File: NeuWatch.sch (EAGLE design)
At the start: 70 parts, among them IC1 SAMD21G18A-AUT, IC3 TPS2115, IC4 SIP32401A, IC5 MC74VHC1G14DFT, T2 2N7002_ALT, Y1 32,768Khz

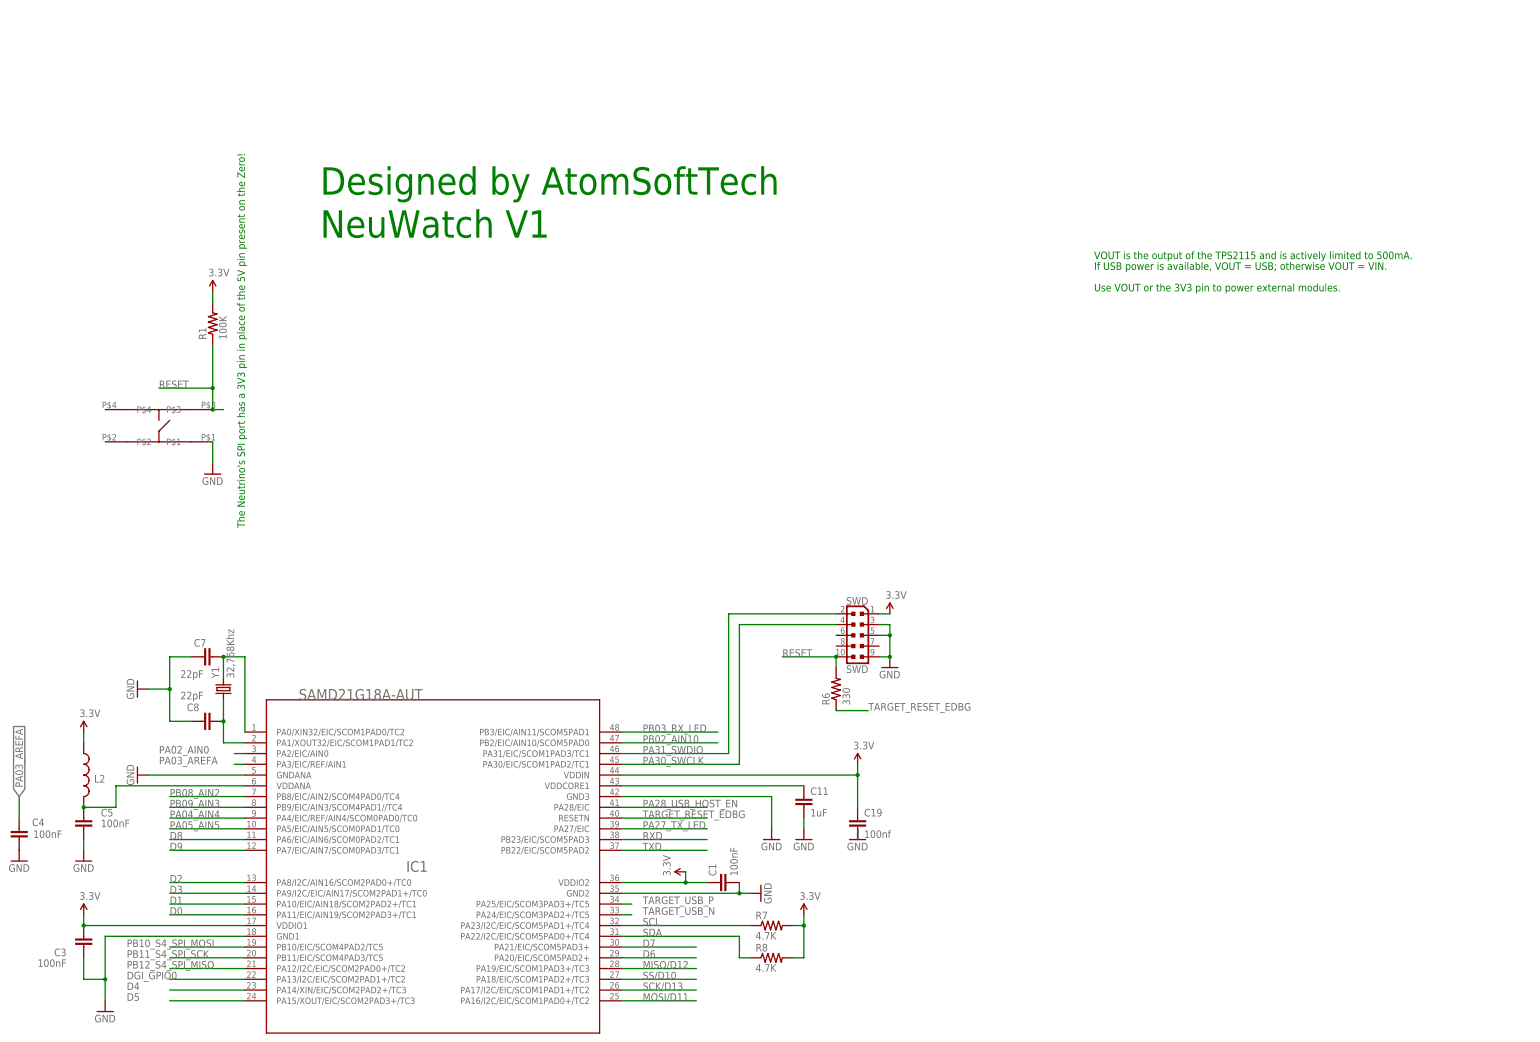
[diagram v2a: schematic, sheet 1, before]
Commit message: Fixes
I2C removed and resistors for buttons changed.
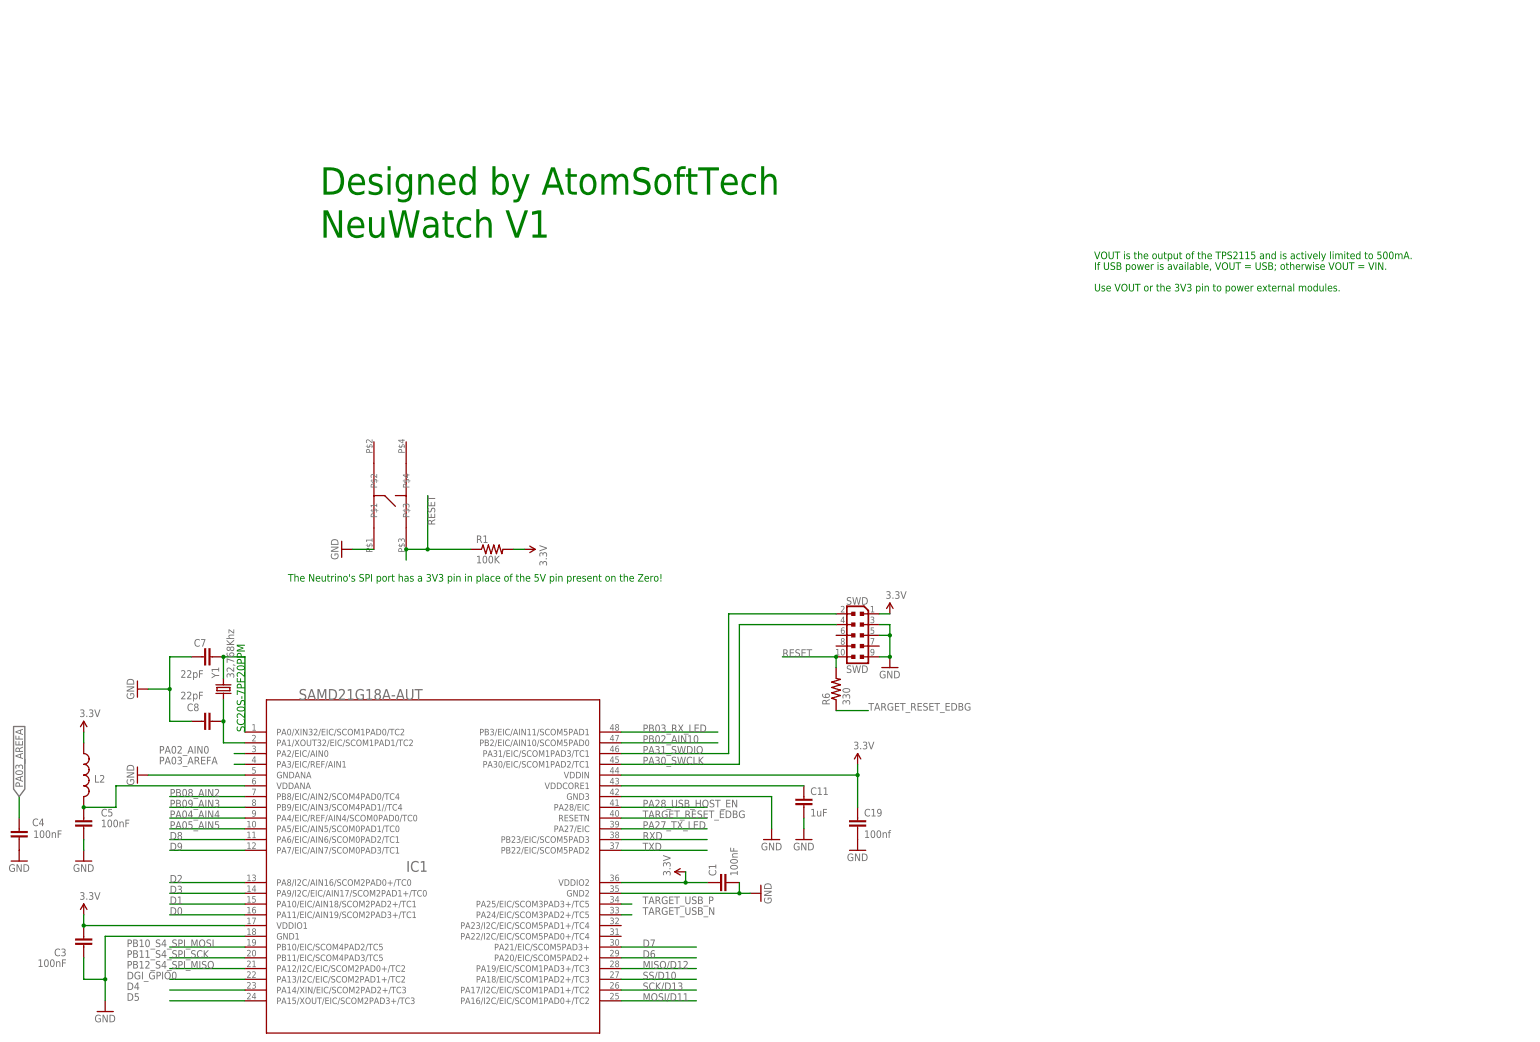
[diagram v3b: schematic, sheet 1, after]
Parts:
- removed R7, R8: 4.7K, adafruit:R-US_R0402
- C10, C15, C16, C9: value (none) -> 100nf
- R13, R14, R15, R16: value (none) -> 47k
- R24: value 5.6k -> 5.6k
- T1: value (none) -> 846
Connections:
- removed net SCL: IC1.PA23/I2C/EIC/SCOM5PAD1+/TC4, R7.1
- removed net SDA: IC1.PA22/I2C/EIC/SCOM5PAD0+/TC4, R8.1
- net 3.3V: no longer R7.2, R8.2
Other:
- note added: "SC20S-7PF20PPM"
- moved on the sheet: R1
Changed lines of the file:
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@@
 <part name="C7" library="AtomTech" deviceset="CAPACITOR" device="C0402" value="22pF"/>
 <part name="C8" library="AtomTech" deviceset="CAPACITOR" device="C0402" value="22pF"/>
-<part name="R7" library="adafruit" deviceset="R-US_" device="R0402" value="4.7K"/>
-<part name="R8" library="adafruit" deviceset="R-US_" device="R0402" value="4.7K"/>
 <part name="C6" library="AtomTech" deviceset="CAPACITOR" device="C0402" value="100nF"/>
 <part name="GND46" library="supply1" deviceset="GND" device=""/>
@@
 <part name="SUPPLY9" library="SparkFun-Aesthetics" deviceset="3.3V" device=""/>
 <part name="SUPPLY10" library="SparkFun-Aesthetics" deviceset="3.3V" device=""/>
-<part name="SUPPLY11" library="SparkFun-Aesthetics" deviceset="3.3V" device=""/>
 <part name="SUPPLY12" library="SparkFun-Aesthetics" deviceset="3.3V" device=""/>
 <part name="SUPPLY13" library="SparkFun-Aesthetics" deviceset="3.3V" device=""/>
@@
 <part name="GND19" library="supply1" deviceset="GND" device=""/>
 <part name="SUPPLY19" library="SparkFun-Aesthetics" deviceset="3.3V" device=""/>
-<part name="R13" library="rcl" deviceset="R-EU_" device="R0402"/>
-<part name="R14" library="rcl" deviceset="R-EU_" device="R0402"/>
-<part name="R15" library="rcl" deviceset="R-EU_" device="R0402"/>
-<part name="R16" library="rcl" deviceset="R-EU_" device="R0402"/>
-<part name="C9" library="AtomTech" deviceset="CAPACITOR" device="C0402"/>
-<part name="C10" library="AtomTech" deviceset="CAPACITOR" device="C0402"/>
-<part name="C15" library="AtomTech" deviceset="CAPACITOR" device="C0402"/>
-<part name="C16" library="AtomTech" deviceset="CAPACITOR" device="C0402"/>
+<part name="R13" library="rcl" deviceset="R-EU_" device="R0402" value="47k"/>
+<part name="R14" library="rcl" deviceset="R-EU_" device="R0402" value="47k"/>
+<part name="R15" library="rcl" deviceset="R-EU_" device="R0402" value="47k"/>
+<part name="R16" library="rcl" deviceset="R-EU_" device="R0402" value="47k"/>
+<part name="C9" library="AtomTech" deviceset="CAPACITOR" device="C0402" value="100nf"/>
+<part name="C10" library="AtomTech" deviceset="CAPACITOR" device="C0402" value="100nf"/>
+<part name="C15" library="AtomTech" deviceset="CAPACITOR" device="C0402" value="100nf"/>
+<part name="C16" library="AtomTech" deviceset="CAPACITOR" device="C0402" value="100nf"/>
 <part name="U$1" library="AtomTech" deviceset="ADXL335" device=""/>
 <part name="SUPPLY5" library="SparkFun-Aesthetics" deviceset="3.3V" device=""/>
@@
 <part name="R22" library="rcl" deviceset="R-EU_" device="R0402" value="47k"/>
 <part name="R23" library="rcl" deviceset="R-EU_" device="R0402" value="150k"/>
-<part name="T1" library="transistor" deviceset="*-NPN-" device="SOT23-BEC" technology="BC846BLT1"/>
-<part name="R24" library="rcl" deviceset="R-EU_" device="R0402" value="5.6k"/>
+<part name="T1" library="transistor" deviceset="*-NPN-" device="SOT23-BEC" technology="BC846BLT1" value="846"/>
+<part name="R24" library="rcl" deviceset="R-EU_" device="R0402" value="5.6k "/>
 <part name="T2" library="AtomTech" deviceset="2N7002_ALT" device=""/>
 <part name="SUPPLY3" library="SparkFun-Aesthetics" deviceset="VIN" device=""/>
@@
 <sheet>
 <plain>
-<text x="86.36" y="165.1" size="1.778" layer="91" rot="R90">The Neutrino's SPI port has a 3V3 pin in place of the 5V pin present on the Zero!</text>
+<text x="96.52" y="152.4" size="1.778" layer="91">The Neutrino's SPI port has a 3V3 pin in place of the 5V pin present on the Zero!</text>
 <text x="287.02" y="228.6" size="1.778" layer="91">VOUT is the output of the TPS2115 and is actively limited to 500mA.</text>
 <text x="287.02" y="226.06" size="1.778" layer="91">If USB power is available, VOUT = USB; otherwise VOUT = VIN.</text>
@@
 <text x="104.14" y="243.84" size="6.4516" layer="91">Designed by AtomSoftTech</text>
 <text x="104.14" y="233.68" size="6.4516" layer="91">NeuWatch V1</text>
+<text x="86.36" y="116.84" size="1.9304" layer="91" rot="R90">SC20S-7PF20PPM</text>
 </plain>
 <instances>
@@
 <instance part="C11" gate="G$1" x="218.44" y="101.6"/>
 <instance part="GND38" gate="1" x="218.44" y="91.44"/>
-<instance part="GND40" gate="1" x="231.14" y="91.44"/>
+<instance part="GND40" gate="1" x="231.14" y="88.9"/>
 <instance part="C5" gate="G$1" x="48.26" y="96.52" smashed="yes">
 <attribute name="NAME" x="52.324" y="96.901" size="1.778" layer="95"/>
@@
 <attribute name="VALUE" x="71.12" y="124.587" size="1.778" layer="96"/>
 </instance>
-<instance part="R7" gate="G$1" x="210.82" y="71.12"/>
-<instance part="R8" gate="G$1" x="210.82" y="63.5"/>
 <instance part="GND25" gate="1" x="238.76" y="132.08"/>
 <instance part="R6" gate="G$1" x="226.06" y="127" rot="R90"/>
 <instance part="C1" gate="G$1" x="198.12" y="81.28" rot="R90"/>
-<instance part="R1" gate="G$1" x="78.74" y="213.36" rot="R90"/>
+<instance part="R1" gate="G$1" x="144.78" y="160.02"/>
 <instance part="C3" gate="G$1" x="48.26" y="66.04" smashed="yes" rot="R180">
 <attribute name="NAME" x="44.196" y="65.659" size="1.778" layer="95" rot="R180"/>
@@
 <instance part="GND6" gate="1" x="33.02" y="86.36"/>
 <instance part="U$5" gate="G$1" x="0" y="0"/>
-<instance part="GND11" gate="1" x="78.74" y="177.8"/>
+<instance part="GND11" gate="1" x="109.22" y="160.02" rot="R270"/>
 <instance part="Y1" gate="G$1" x="81.28" y="127" rot="R90"/>
 <instance part="L2" gate="G$1" x="48.26" y="106.68" smashed="yes">
@@
 </instance>
 <instance part="SWD" gate="G$1" x="231.14" y="139.7" rot="MR0"/>
-<instance part="SUPPLY7" gate="G$1" x="78.74" y="220.98"/>
+<instance part="SUPPLY7" gate="G$1" x="152.4" y="160.02" rot="R270"/>
 <instance part="SUPPLY8" gate="G$1" x="238.76" y="144.78"/>
 <instance part="SUPPLY9" gate="G$1" x="231.14" y="109.22"/>
 <instance part="SUPPLY10" gate="G$1" x="190.5" y="83.82" rot="R90"/>
-<instance part="SUPPLY11" gate="G$1" x="218.44" y="73.66"/>
 <instance part="SUPPLY12" gate="G$1" x="48.26" y="73.66"/>
 <instance part="SUPPLY13" gate="G$1" x="48.26" y="116.84"/>
 <instance part="GND16" gate="1" x="60.96" y="127" rot="R270"/>
 <instance part="GND17" gate="1" x="60.96" y="106.68" rot="R270"/>
-<instance part="RESET" gate="G$1" x="63.5" y="187.96" rot="R180"/>
+<instance part="RESET" gate="G$1" x="119.38" y="175.26" rot="R90"/>
 <instance part="C19" gate="G$1" x="231.14" y="96.52"/>
 </instances>
@@
 <pinref part="GND40" gate="1" pin="GND"/>
 <pinref part="C19" gate="G$1" pin="2"/>
-<wire x1="231.14" y1="93.98" x2="231.14" y2="91.44" width="0.1524" layer="91"/>
 </segment>
 <segment>
@@
 </segment>
 <segment>
-<wire x1="78.74" y1="185.42" x2="78.74" y2="180.34" width="0.1524" layer="91"/>
+<wire x1="116.84" y1="160.02" x2="111.76" y2="160.02" width="0.1524" layer="91"/>
 <pinref part="GND11" gate="1" pin="GND"/>
 <pinref part="RESET" gate="G$1" pin="P$1"/>
@@
 <net name="RESET" class="0">
 <segment>
-<label x="66.04" y="198.12" size="1.778" layer="95"/>
-<wire x1="78.74" y1="198.12" x2="78.74" y2="208.28" width="0.1524" layer="91"/>
+<label x="129.54" y="172.72" size="1.778" layer="95" rot="R270"/>
+<wire x1="129.54" y1="160.02" x2="139.7" y2="160.02" width="0.1524" layer="91"/>
 <pinref part="R1" gate="G$1" pin="1"/>
-<wire x1="81.28" y1="193.04" x2="78.74" y2="193.04" width="0.1524" layer="91"/>
-<wire x1="78.74" y1="193.04" x2="78.74" y2="198.12" width="0.1524" layer="91"/>
-<junction x="78.74" y="198.12"/>
-<wire x1="78.74" y1="198.12" x2="66.04" y2="198.12" width="0.1524" layer="91"/>
+<wire x1="124.46" y1="157.48" x2="124.46" y2="160.02" width="0.1524" layer="91"/>
+<wire x1="124.46" y1="160.02" x2="129.54" y2="160.02" width="0.1524" layer="91"/>
+<junction x="129.54" y="160.02"/>
+<wire x1="129.54" y1="160.02" x2="129.54" y2="172.72" width="0.1524" layer="91"/>
 <pinref part="RESET" gate="G$1" pin="P$3"/>
-<junction x="78.74" y="193.04"/>
+<junction x="124.46" y="160.02"/>
 </segment>
 <segment>
@@
 <net name="3.3V" class="0">
 <segment>
-<wire x1="78.74" y1="218.44" x2="78.74" y2="220.98" width="0.1524" layer="91"/>
+<wire x1="149.86" y1="160.02" x2="152.4" y2="160.02" width="0.1524" layer="91"/>
 <pinref part="R1" gate="G$1" pin="2"/>
 <pinref part="SUPPLY7" gate="G$1" pin="3.3V"/>
@@
 </segment>
 <segment>
-<pinref part="R7" gate="G$1" pin="2"/>
-<wire x1="215.9" y1="71.12" x2="218.44" y2="71.12" width="0.1524" layer="91"/>
-<pinref part="R8" gate="G$1" pin="2"/>
-<wire x1="218.44" y1="71.12" x2="218.44" y2="63.5" width="0.1524" layer="91"/>
-<wire x1="218.44" y1="63.5" x2="215.9" y2="63.5" width="0.1524" layer="91"/>
-<wire x1="218.44" y1="71.12" x2="218.44" y2="73.66" width="0.1524" layer="91"/>
-<junction x="218.44" y="71.12"/>
-<pinref part="SUPPLY11" gate="G$1" pin="3.3V"/>
-</segment>
-<segment>
 <wire x1="236.22" y1="144.78" x2="238.76" y2="144.78" width="0.1524" layer="91"/>
 <pinref part="SWD" gate="G$1" pin="1"/>
@@
 </segment>
 </net>
-<net name="SDA" class="0">
-<segment>
-<pinref part="IC1" gate="G$1" pin="PA22/I2C/EIC/SCOM5PAD0+/TC4"/>
-<wire x1="175.26" y1="68.58" x2="203.2" y2="68.58" width="0.1524" layer="91"/>
-<wire x1="203.2" y1="68.58" x2="203.2" y2="63.5" width="0.1524" layer="91"/>
-<wire x1="203.2" y1="63.5" x2="205.74" y2="63.5" width="0.1524" layer="91"/>
-<label x="180.34" y="68.58" size="1.778" layer="95"/>
-<pinref part="R8" gate="G$1" pin="1"/>
-</segment>
-</net>
-<net name="SCL" class="0">
-<segment>
-<pinref part="IC1" gate="G$1" pin="PA23/I2C/EIC/SCOM5PAD1+/TC4"/>
-<wire x1="175.26" y1="71.12" x2="205.74" y2="71.12" width="0.1524" layer="91"/>
-<label x="180.34" y="71.12" size="1.778" layer="95"/>
-<pinref part="R7" gate="G$1" pin="1"/>
-</segment>
-</net>

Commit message: small fixes
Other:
- note added: "A0"
- note added: "A1"
- note added: "A2"
- note added: "A3"
- note added: "A4"
- note removed: "AIN4 == A3"
- note removed: "AIN5 == A4"
- moved on the sheet: C1, C11, C19, C3, C4, C5, C7, C8, IC1, L2, R1, R6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

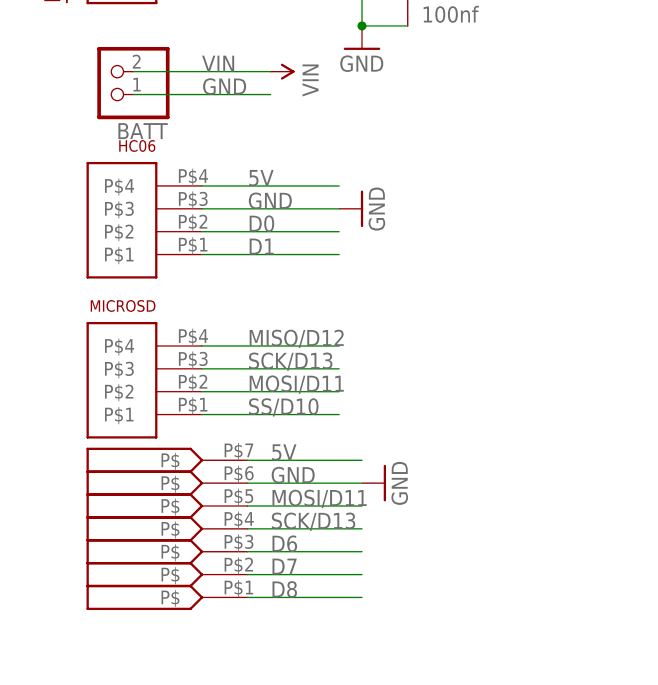
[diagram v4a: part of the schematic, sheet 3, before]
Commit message: removed boost and others
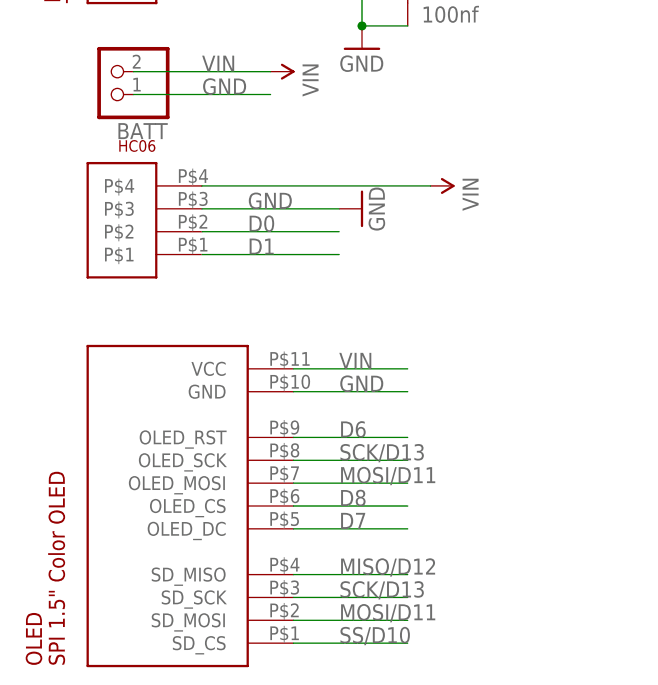
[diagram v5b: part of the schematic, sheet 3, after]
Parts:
- removed BOOST: TPS6102X, AtomTech:TPS6102X
- removed C17: 10 uF, AtomTech:CAPACITORC0402
- removed C18: 47uf, AtomTech:CAPACITORC0402
- removed L3: 6.8 uH, Bourns_By_element14_Batch_1:PM0603-R12J-RC
- removed MICROSD: 1X4, AtomTech:1X4
- removed R17, R18, R19: 100K, adafruit:R-US_R0402
- OLED: value 1X7 -> 1.5-OLED; device AtomTech:1X7 -> AtomTech:1.5-OLED
- SWD: value SWD -> PINHEAD-2x5-P1.27; device AtomTech:DEBUG_10P_SMT -> Neutrino-:ARDUINO-NEUTRINO-082_CONNETTORI_0171_PH127-205DF055G00A
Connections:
- removed net 5V: BOOST.VOUT, C18.1, HC06.P$4, OLEDG$7.P$, R17.2
- removed net LBI: BOOST.LBI, R18.1, R19.2
- removed net LBO: BOOST.LBO, R17.1
- removed net SW: BOOST.SW, L3.2
- net D6: now also OLED.OLED_RST; no longer OLEDG$3.P$
- net D7: now also OLED.OLED_DC; no longer OLEDG$2.P$
- net D8: now also OLED.OLED_CS; no longer OLEDG$1.P$
- net GND: now also OLED.GND; no longer BOOST.GND, BOOST.PGND, BOOST.PS, C17.2, C18.2, OLEDG$6.P$, R19.1
- net MISO/D12: now also OLED.SD_MISO; no longer MICROSD.P$4
- net MOSI/D11: now also OLED.OLED_MOSI, OLED.SD_MOSI; no longer MICROSD.P$2, OLEDG$5.P$
- net SCK/D13: now also OLED.OLED_SCK, OLED.SD_SCK; no longer MICROSD.P$3, OLEDG$4.P$
- net SS/D10: now also OLED.SD_CS; no longer MICROSD.P$1
- net VIN: now also HC06.P$4, OLED.VCC
- net VMAIN: no longer BOOST.EN, BOOST.VBAT, C17.1, L3.1, R18.2
